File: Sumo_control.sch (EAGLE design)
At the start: 14 parts, among them X1 MICROMATCH-8

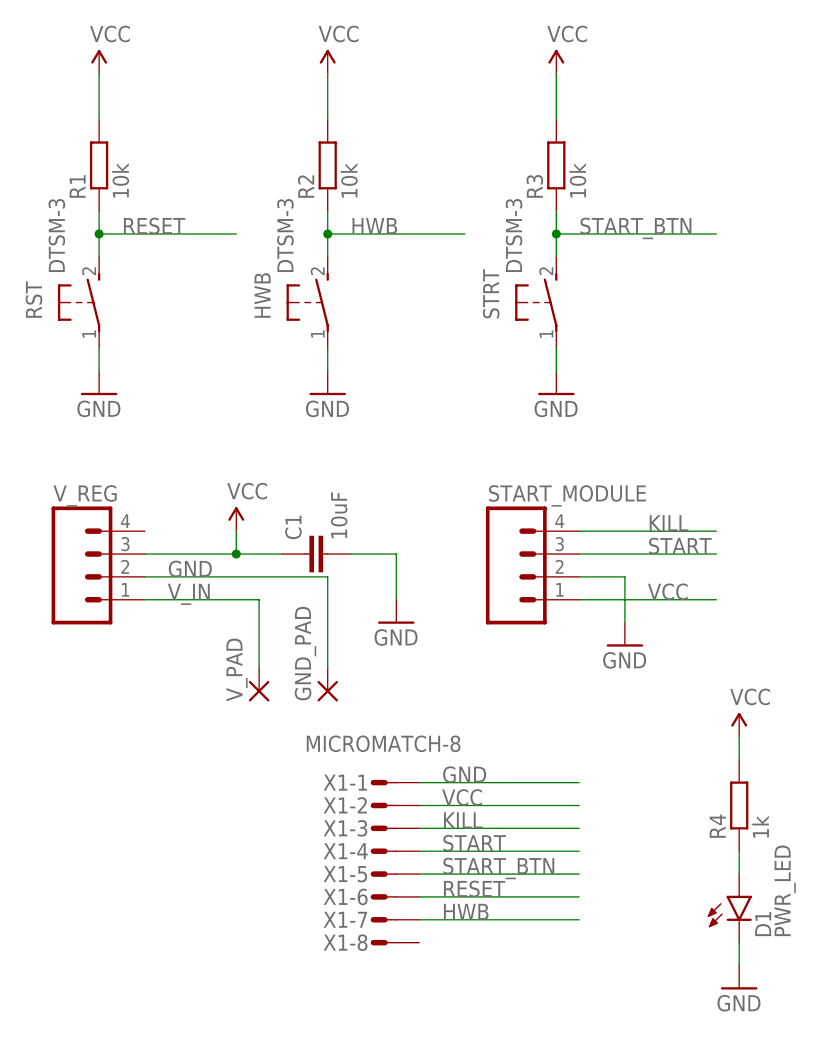
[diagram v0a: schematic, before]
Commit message: Replace power pads with bigger ones
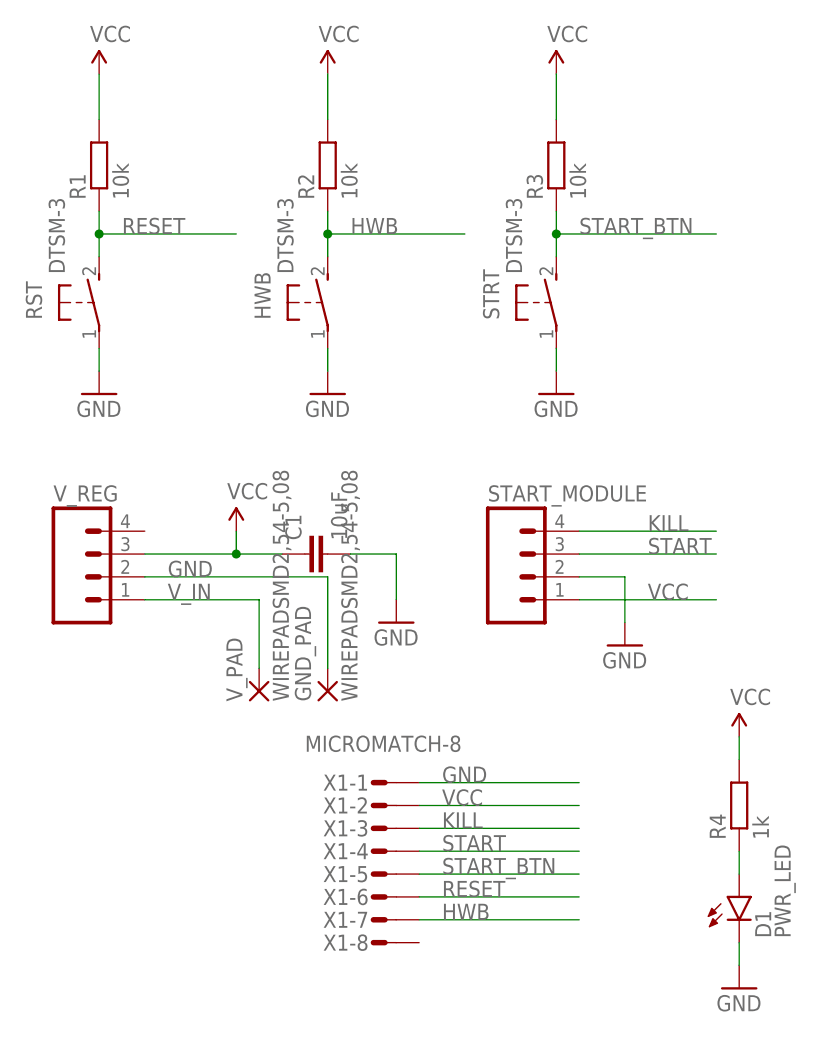
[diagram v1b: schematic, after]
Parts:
- GND_PAD, V_PAD: value (none) -> WIREPADSMD2,54-5,08; device wirepad:SMD2 -> wirepad:WIREPADSMD2,54-5,08
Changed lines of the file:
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@@
 <part name="GND6" library="SparkFun-Aesthetics" deviceset="GND" device=""/>
 <part name="SUPPLY5" library="SparkFun-Aesthetics" deviceset="VCC" device=""/>
-<part name="GND_PAD" library="wirepad" deviceset="SMD2" device=""/>
-<part name="V_PAD" library="wirepad" deviceset="SMD2" device=""/>
+<part name="GND_PAD" library="wirepad" deviceset="WIREPAD" device="SMD2,54-5,08"/>
+<part name="V_PAD" library="wirepad" deviceset="WIREPAD" device="SMD2,54-5,08"/>
 </parts>
 <sheets>
@@
 <instance part="GND6" gate="1" x="91.44" y="-55.88"/>
 <instance part="SUPPLY5" gate="G$1" x="91.44" y="-27.94"/>
-<instance part="GND_PAD" gate="1" x="45.72" y="-22.86" rot="R90"/>
-<instance part="V_PAD" gate="1" x="38.1" y="-22.86" rot="R90"/>
+<instance part="GND_PAD" gate="G$1" x="45.72" y="-22.86" rot="R90"/>
+<instance part="V_PAD" gate="G$1" x="38.1" y="-22.86" rot="R90"/>
 </instances>
 <busses>
@@
 <label x="27.94" y="-10.16" size="1.778" layer="95"/>
 <wire x1="45.72" y1="-20.32" x2="45.72" y2="-10.16" width="0.1524" layer="91"/>
-<pinref part="GND_PAD" gate="1" pin="P"/>
+<pinref part="GND_PAD" gate="G$1" pin="P"/>
 </segment>
 <segment>
@@
 <label x="27.94" y="-12.7" size="1.778" layer="95"/>
 <wire x1="38.1" y1="-20.32" x2="38.1" y2="-12.7" width="0.1524" layer="91"/>
-<pinref part="V_PAD" gate="1" pin="P"/>
+<pinref part="V_PAD" gate="G$1" pin="P"/>
 </segment>
 </net>
